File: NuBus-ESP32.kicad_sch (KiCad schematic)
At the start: 21 parts, among them J2 Xunpu TF-115, J3 microUSB-B, U27 AZ1117EH-3.3TRG1

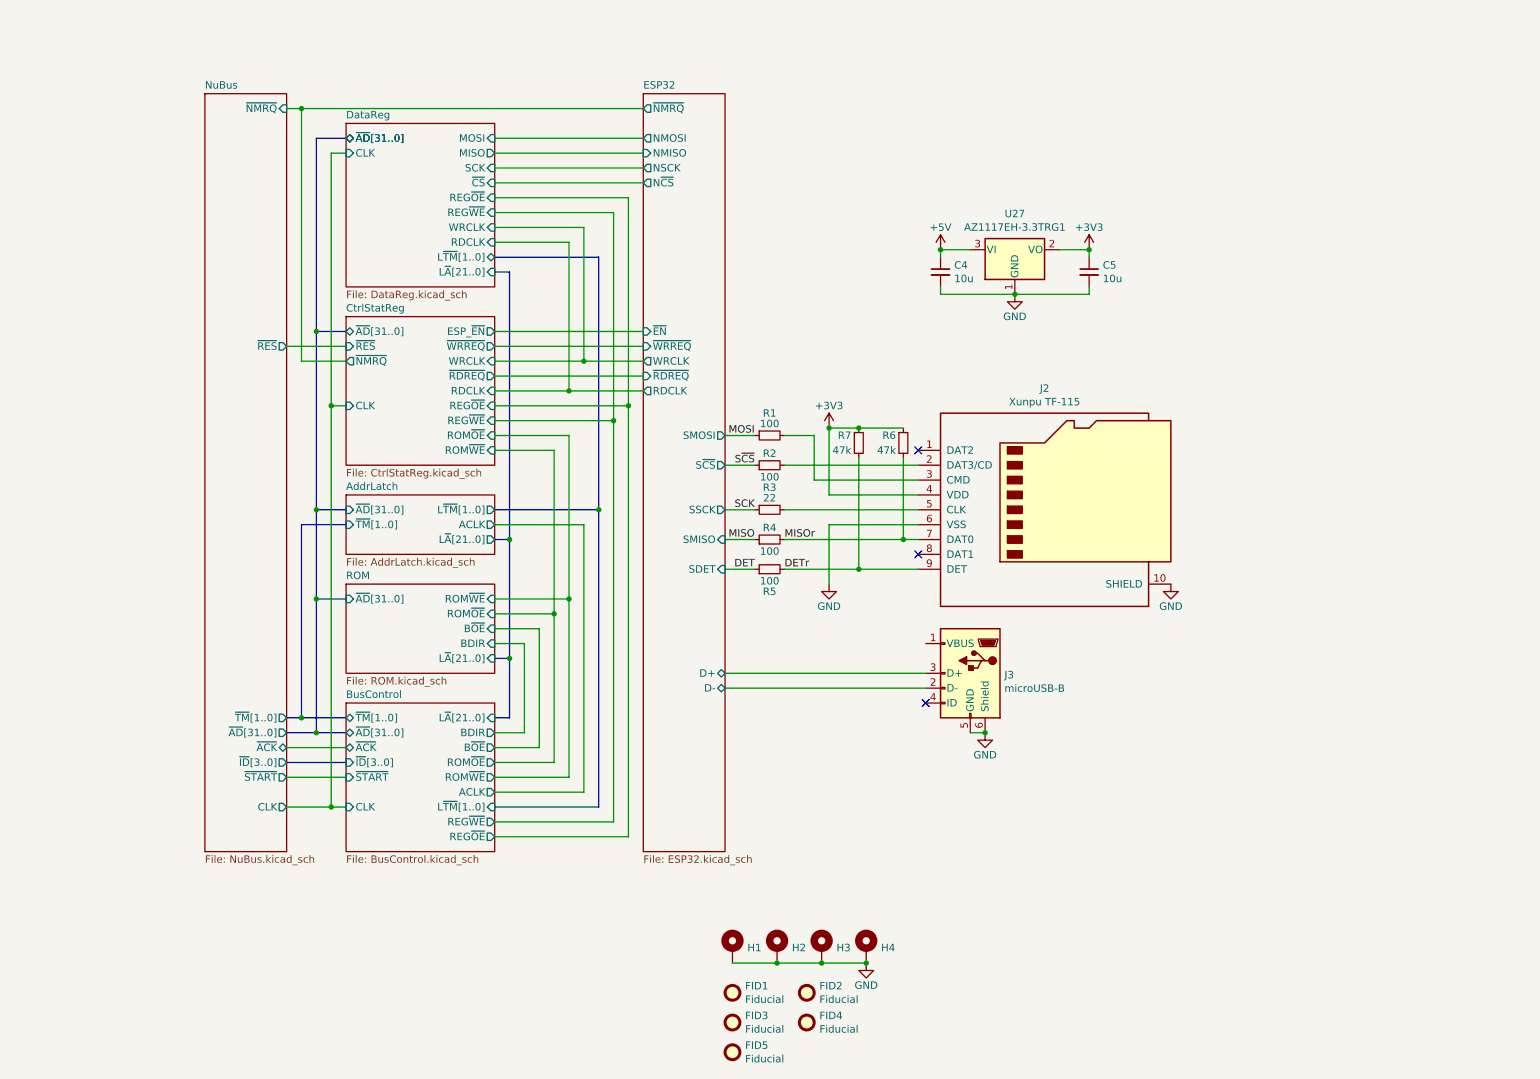
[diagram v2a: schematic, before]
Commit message: Prototype with 74xx
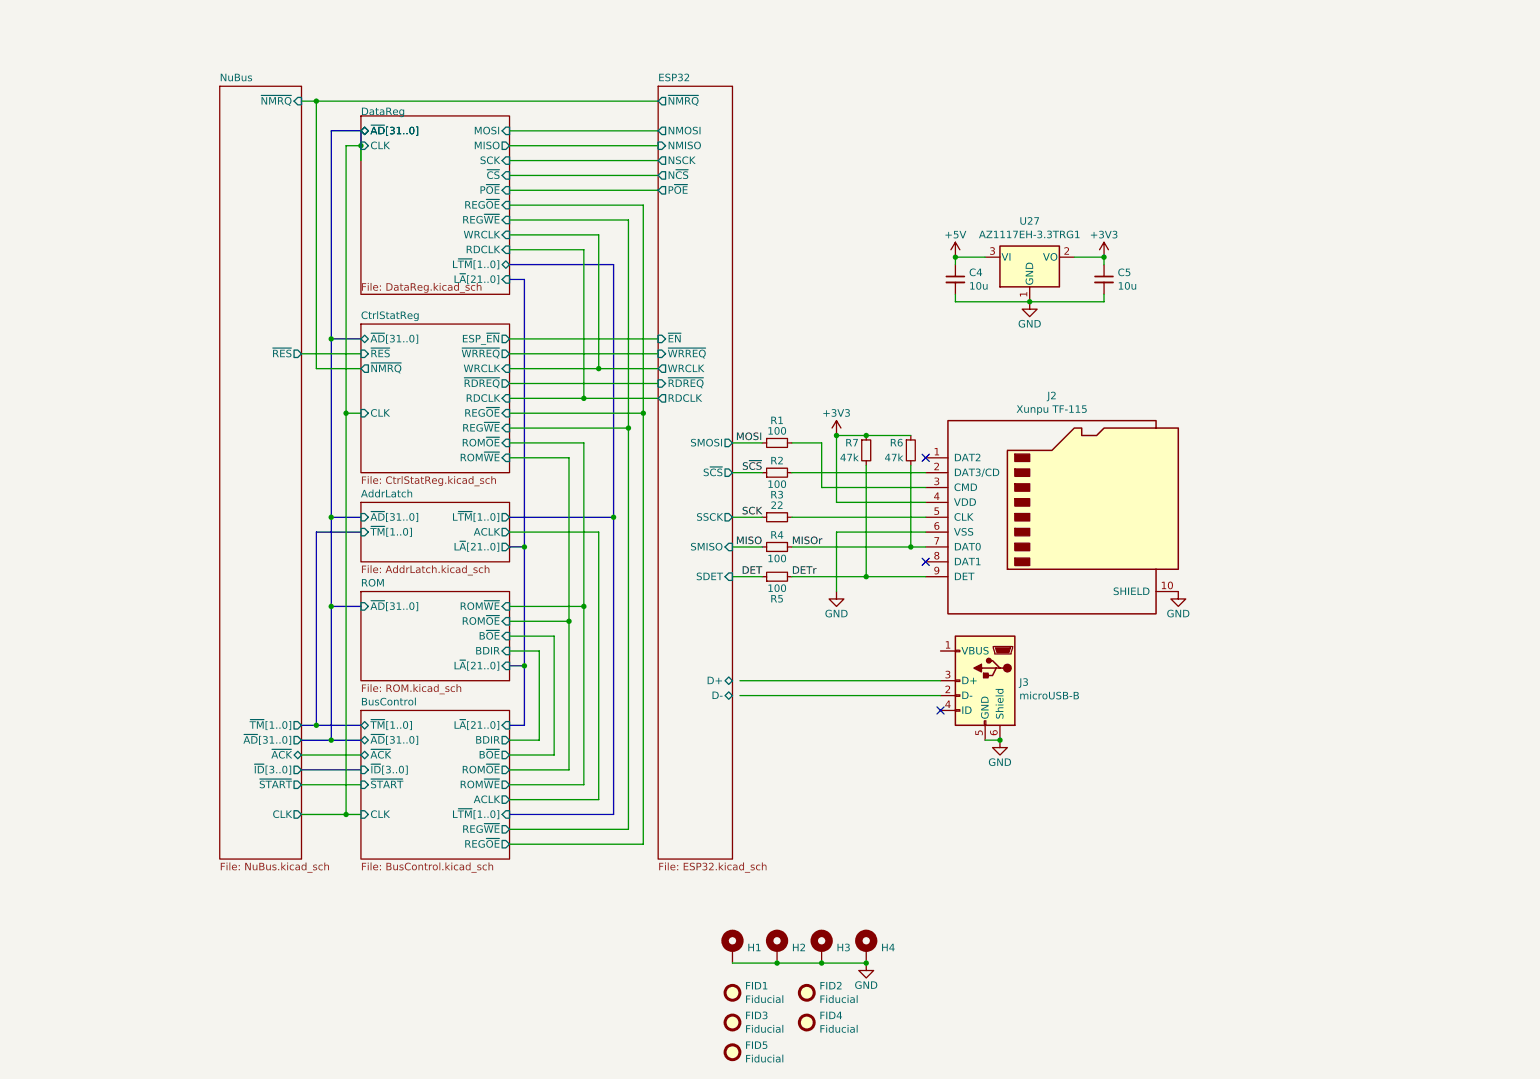
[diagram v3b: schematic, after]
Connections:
- net ESP32/D+: no longer J3.3 (D+)
- net ESP32/D-: no longer J3.2 (D-)
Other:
- sheet DataReg ports: added P~{OE}; removed none
- sheet ESP32 ports: added P~{OE}; removed none
- moved on the sheet: C4, C5, J2, J3, R1, R2, R3, R4, R5, R6, R7, U27

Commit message: work on FPGA
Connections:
- net ESP32/D+: now also J3.3 (D+)
- net ESP32/D-: now also J3.2 (D-)
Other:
- removed sheet AddrLatch
- removed sheet BusControl
- removed sheet CtrlStatReg
- removed sheet DataReg
- added sheet Buf (Buf.kicad_sch)
- added sheet FPGA (FPGA.kicad_sch)
- sheet ESP32 ports: added C~{CS}, FPGA_TDO, F~{CS}, J~{CS}, R~{CS}, W~{CS}, ~{IRQ}; removed N~{CS}, P~{OE}, RDCLK, WRCLK, ~{EN}, ~{NMRQ}
- sheet ROM ports: added D2, D3, M0SI, M1SO, SCK0, SCK1, ~{CS}0, ~{CS}1; removed BDIR, B~{OE}, L~{A}[21..0], ROM~{OE}, ROM~{WE}, ~{AD}[31..0]
- moved on the sheet: C4, C5, J2, J3, R1, R2, R3, R4, R5, R6, R7, U27

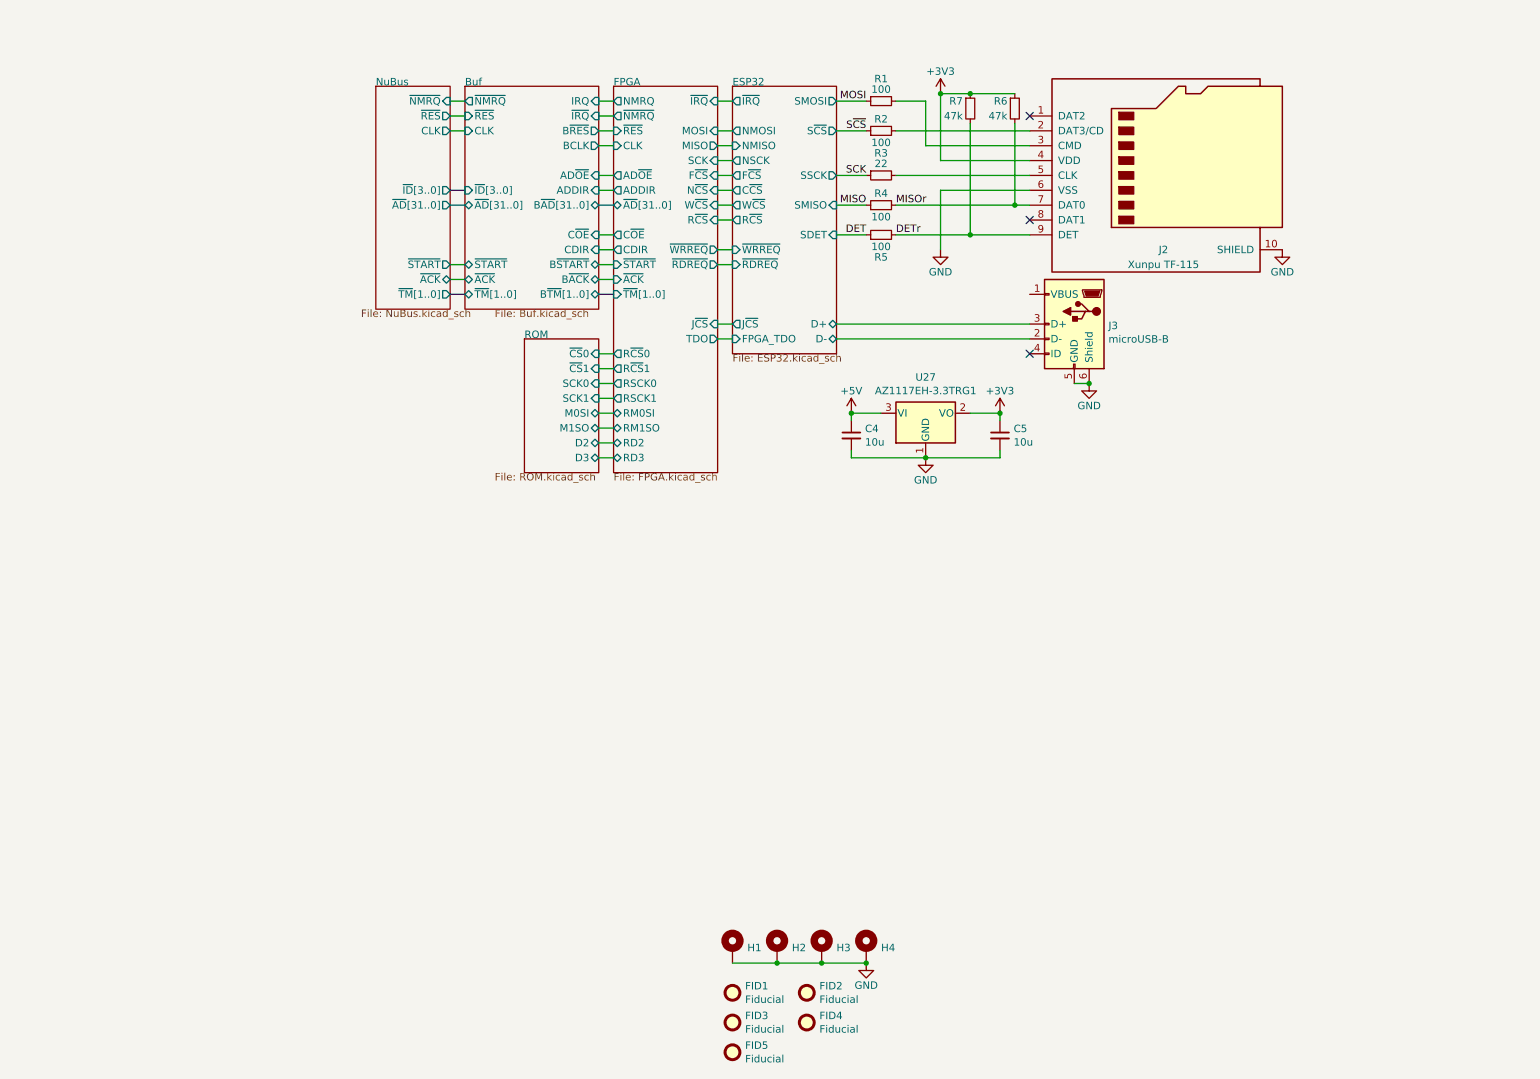
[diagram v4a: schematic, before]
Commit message: Revert "work on FPGA"
This reverts commit a96523e8d17974c7c48efc8a38ae046f7948cd49.
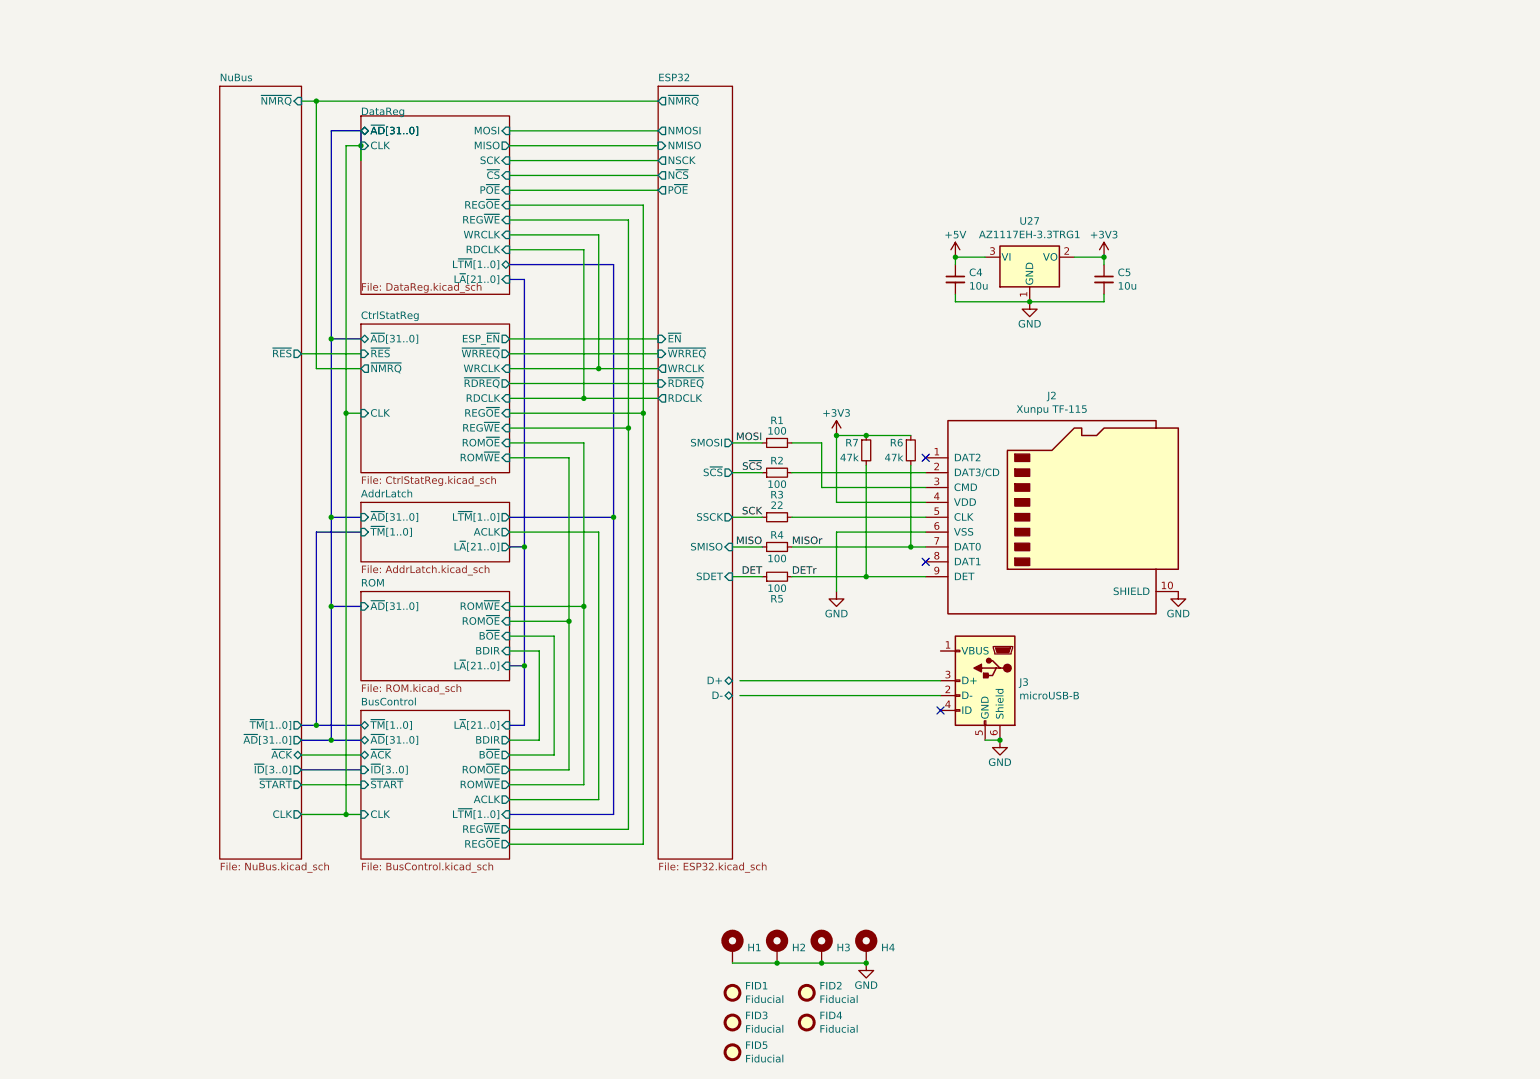
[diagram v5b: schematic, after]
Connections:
- net ESP32/D+: no longer J3.3 (D+)
- net ESP32/D-: no longer J3.2 (D-)
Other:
- removed sheet Buf
- removed sheet FPGA
- added sheet AddrLatch (AddrLatch.kicad_sch)
- added sheet BusControl (BusControl.kicad_sch)
- added sheet CtrlStatReg (CtrlStatReg.kicad_sch)
- added sheet DataReg (DataReg.kicad_sch)
- sheet ESP32 ports: added N~{CS}, P~{OE}, RDCLK, WRCLK, ~{EN}, ~{NMRQ}; removed C~{CS}, FPGA_TDO, F~{CS}, J~{CS}, R~{CS}, W~{CS}, ~{IRQ}
- sheet ROM ports: added BDIR, B~{OE}, L~{A}[21..0], ROM~{OE}, ROM~{WE}, ~{AD}[31..0]; removed D2, D3, M0SI, M1SO, SCK0, SCK1, ~{CS}0, ~{CS}1
- moved on the sheet: C4, C5, J2, J3, R1, R2, R3, R4, R5, R6, R7, U27

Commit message: idk
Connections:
- net ESP32/D+: now also J3.3 (D+)
- net ESP32/D-: now also J3.2 (D-)
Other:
- moved on the sheet: J3
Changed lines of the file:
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@@
   (junction (at 68.58 27.94) (diameter 0) (color 0 0 0 0)
   )
-  (junction (at 76.2 35.56) (diameter 0) (color 0 0 0 0)
-  )
   (junction (at 121.92 83.82) (diameter 0) (color 0 0 0 0)
   )
@@
   (junction (at 157.48 85.09) (diameter 0) (color 0 0 0 0)
   )
-  (junction (at 185.42 137.16) (diameter 0) (color 0 0 0 0)
+  (junction (at 184.15 137.16) (diameter 0) (color 0 0 0 0)
   )
   (junction (at 71.12 114.3) (diameter 0) (color 0 0 0 0)
@@
   )
   (no_connect (at 172.72 106.68))
-  (no_connect (at 175.26 132.08))
+  (no_connect (at 173.99 132.08))
   (no_connect (at 172.72 88.9))
   (wire (pts (xy 139.7 91.44) (xy 144.78 91.44))
@@
     (stroke (width 0) (type default) (color 0 0 0 0))
   )
-  (bus (pts (xy 76.2 33.02) (xy 76.2 35.56))
-    (stroke (width 0) (type default) (color 0 0 0 0))
-  )
   (wire (pts (xy 101.6 152.4) (xy 121.92 152.4))
     (stroke (width 0) (type default) (color 0 0 0 0))
@@
     (stroke (width 0) (type default) (color 0 0 0 0))
   )
-  (wire (pts (xy 185.42 137.16) (xy 182.88 137.16))
+  (wire (pts (xy 184.15 137.16) (xy 181.61 137.16))
     (stroke (width 0) (type default) (color 0 0 0 0))
   )
@@
     (stroke (width 0) (type default) (color 0 0 0 0))
   )
-  (wire (pts (xy 175.26 129.54) (xy 140.97 129.54))
+  (wire (pts (xy 173.99 129.54) (xy 139.7 129.54))
     (stroke (width 0) (type default) (color 0 0 0 0))
   )
@@
     (stroke (width 0) (type default) (color 0 0 0 0))
   )
-  (wire (pts (xy 175.26 127) (xy 140.97 127))
+  (wire (pts (xy 173.99 127) (xy 139.7 127))
     (stroke (width 0) (type default) (color 0 0 0 0))
   )
@@
   )
   (wire (pts (xy 109.22 119.38) (xy 109.22 139.7))
-    (stroke (width 0) (type default) (color 0 0 0 0))
-  )
-  (wire (pts (xy 76.2 35.56) (xy 76.2 38.1))
     (stroke (width 0) (type default) (color 0 0 0 0))
   )
@@
     (pin "2")
   )
-  (symbol (lib_id "Connector:USB_B_Micro") (at 182.88 127 0) (mirror y) (unit 1)
-    (in_bom yes) (on_board yes)
-    (property "Reference" "J3" (id 0) (at 188.722 127.2794 0)
-      (effects (font (size 1.27 1.27)) (justify right))
-    )
-    (property "Value" "microUSB-B" (id 1) (at 188.722 129.5908 0)
-      (effects (font (size 1.27 1.27)) (justify right))
-    )
-    (property "Footprint" "stdpads:USB_Micro-B_ShouHan_MicroXNJ" (id 2) (at 179.07 128.27 0)
-      (effects (font (size 1.27 1.27)) hide)
-    )
-    (property "Datasheet" "~" (id 3) (at 179.07 128.27 0)
-      (effects (font (size 1.27 1.27)) hide)
-    )
-    (property "LCSC Part" "C404969" (id 4) (at 182.88 127 0)
+  (symbol (lib_id "Connector:USB_B_Micro") (at 181.61 127 0) (mirror y) (unit 1)
+    (in_bom yes) (on_board yes)
+    (property "Reference" "J3" (id 0) (at 187.452 127.2794 0)
+      (effects (font (size 1.27 1.27)) (justify right))
+    )
+    (property "Value" "microUSB-B" (id 1) (at 187.452 129.5908 0)
+      (effects (font (size 1.27 1.27)) (justify right))
+    )
+    (property "Footprint" "stdpads:USB_Micro-B_ShouHan_MicroXNJ" (id 2) (at 177.8 128.27 0)
+      (effects (font (size 1.27 1.27)) hide)
+    )
+    (property "Datasheet" "~" (id 3) (at 177.8 128.27 0)
+      (effects (font (size 1.27 1.27)) hide)
+    )
+    (property "LCSC Part" "C404969" (id 4) (at 181.61 127 0)
       (effects (font (size 1.27 1.27)) hide)
     )
@@
     (pin "6")
   )
-  (symbol (lib_id "power:GND") (at 185.42 137.16 0) (unit 1)
-    (in_bom yes) (on_board yes)
-    (property "Reference" "#PWR0101" (id 0) (at 185.42 143.51 0)
-      (effects (font (size 1.27 1.27)) hide)
-    )
-    (property "Value" "GND" (id 1) (at 185.42 140.97 0))
-    (property "Footprint" "" (id 2) (at 185.42 137.16 0)
-      (effects (font (size 1.27 1.27)) hide)
-    )
-    (property "Datasheet" "" (id 3) (at 185.42 137.16 0)
+  (symbol (lib_id "power:GND") (at 184.15 137.16 0) (unit 1)
+    (in_bom yes) (on_board yes)
+    (property "Reference" "#PWR0101" (id 0) (at 184.15 143.51 0)
+      (effects (font (size 1.27 1.27)) hide)
+    )
+    (property "Value" "GND" (id 1) (at 184.15 140.97 0))
+    (property "Footprint" "" (id 2) (at 184.15 137.16 0)
+      (effects (font (size 1.27 1.27)) hide)
+    )
+    (property "Datasheet" "" (id 3) (at 184.15 137.16 0)
       (effects (font (size 1.27 1.27)) hide)
     )
@@
       (effects (font (size 1.27 1.27)) (justify left bottom))
     )
-    (property "Sheet file" "DataReg.kicad_sch" (id 1) (at 76.2 59.0046 0)
+    (property "Sheet file" "DataReg.kicad_sch" (id 1) (at 76.2 60.96 0)
       (effects (font (size 1.27 1.27)) (justify left top))
     )
@@
       (reference "#PWR0236") (unit 1) (value "GND") (footprint "")
     )
+    (path "/00000000-0000-0000-0000-000061d1084d/30c674fb-d4c7-4bf4-b9bf-a6e82e57768f"
+      (reference "#PWR?") (unit 1) (value "GND") (footprint "")
+    )
+    (path "/00000000-0000-0000-0000-000061d1084d/6a179451-6994-4920-b71a-56c4455adeac"
+      (reference "#PWR?") (unit 1) (value "GND") (footprint "")
+    )
+    (path "/00000000-0000-0000-0000-000061d1084d/7fdb9d91-7fd7-45aa-9983-f4642ef05716"
+      (reference "#PWR?") (unit 1) (value "+5V") (footprint "")
+    )
+    (path "/00000000-0000-0000-0000-000061d1084d/c9623ce8-4935-46b4-ab03-4205f87fd5a5"
+      (reference "#PWR?") (unit 1) (value "GND") (footprint "")
+    )
+    (path "/00000000-0000-0000-0000-000061d1084d/cdd9c339-14f4-4918-a592-7669981b1672"
+      (reference "#PWR?") (unit 1) (value "+5V") (footprint "")
+    )
+    (path "/00000000-0000-0000-0000-000061d1084d/cee4ccd6-4aa0-49b3-a32d-6b60c416dabb"
+      (reference "#PWR?") (unit 1) (value "GND") (footprint "")
+    )
     (path "/00000000-0000-0000-0000-000064084316/00000000-0000-0000-0000-0000641a5d54"
       (reference "C1") (unit 1) (value "22p") (footprint "stdpads:C_0805")
@@
       (reference "U42") (unit 5) (value "74LVC32AD") (footprint "stdpads:SOIC-14_3.9mm")
     )
+    (path "/00000000-0000-0000-0000-000061d1084d/14e9aaba-092e-4678-a397-7a189c85b45d"
+      (reference "U?") (unit 1) (value "GAL16V8") (footprint "")
+    )
+    (path "/00000000-0000-0000-0000-000061d1084d/d71a7aac-22b8-4fd1-9339-80300f144536"
+      (reference "U?") (unit 1) (value "GAL16V8") (footprint "")
+    )
     (path "/00000000-0000-0000-0000-000064084316/00000000-0000-0000-0000-0000641a5cd3"
